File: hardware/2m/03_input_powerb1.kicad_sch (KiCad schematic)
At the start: 11 parts, among them Q303 MMBT3904,215

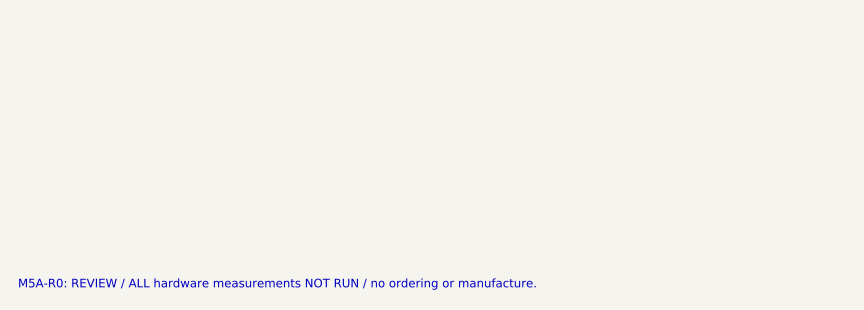
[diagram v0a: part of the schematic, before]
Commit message: Preserve M5A-R1 VHF electrical candidate and review evidence
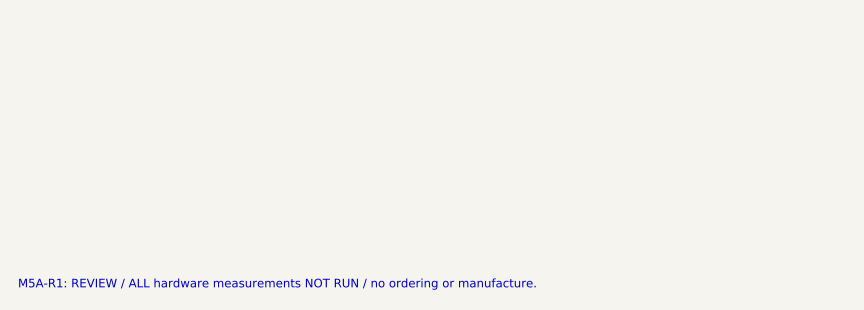
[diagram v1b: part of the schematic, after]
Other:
- note added: "M5A-R1: REVIEW / ALL hardware measurements NOT RUN / no ordering or manufacture."
- note removed: "M5A-R0: REVIEW / ALL hardware measurements NOT RUN / no ordering or manufacture."

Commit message: Preserve M5A-R3 historical transmitter schematic and review
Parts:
- C306: value 22u -> 1u; footprint Capacitor_SMD:C_1210_3225Metric -> Capacitor_SMD:C_0805_2012Metric; Engineering_Note (none) -> R3 switched-rail local1uF; original470uF bulk is upstream o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; MPN GRM32ER71E226KE15L -> CC0805KKX7R9BB105
- R309: Engineering_Note (none) -> 0.1ohm high-side normal-rail sense. Approx0.6A trip. Exact 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
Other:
- note added: "M5A-R3: REVIEW / ALL hardware measurements NOT RUN / no ordering or manufacture."
- note added: "R3: no RF/analog/thermal hardware validation. Original RF attribution and open procurement in M5A_R3 documents."
- note removed: "M5A-R1: REVIEW / ALL hardware measurements NOT RUN / no ordering or manufacture."

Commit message: Preserve M5A-R4 economical VHF electrical review baseline
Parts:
- C306: value 1u -> 100n; footprint Capacitor_SMD:C_0805_2012Metric -> Capacitor_SMD:C_0603_1608Metric; Engineering_Note R3 switched-rail local1uF; original470uF bulk is upstream o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 -> Protected9V local bypass; converter bulk upstream, driver r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; MPN CC0805KKX7R9BB105 -> CC0603KRX7R8BB104
- R309: Engineering_Note 0.1ohm high-side normal-rail sense. Approx0.6A trip. Exact 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 -> High-side0.1ohm sense; nominal1.80A analog trip retained. V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
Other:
- note added: "M5A-R4: REVIEW / ALL hardware measurements NOT RUN / no ordering or manufacture."
- note added: "M5A-R4: hardware measurements NOT_RUN; source/reference and simplification in R4 documents."
- note removed: "M5A-R3: REVIEW / ALL hardware measurements NOT RUN / no ordering or manufacture."
- note removed: "R3: no RF/analog/thermal hardware validation. Original RF attribution and open procurement in M5A_R3 documents."

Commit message: Preserve M5B-E1 integrated RF2M evaluation baseline
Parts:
- R309: value 0.1 -> 0.068; Engineering_Note High-side0.1ohm sense; nominal1.80A analog trip retained. V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 -> M5B confirmed current-protection correction:.068ohm1percent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; MPN OPEN 0.1ohm 1% 1W Kelvin layout -> WSL2512R0680FEA
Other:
- note added: "M5B-E1 / integrated evaluation PCB / NOT RELEASED / hardware tests NOT_RUN"
- note added: "M5B-E1: REVIEW / ALL hardware measurements NOT RUN / no ordering or manufacture."
- note removed: "M5A-R4: REVIEW / ALL hardware measurements NOT RUN / no ordering or manufacture."
- note removed: "M5A-R4: hardware measurements NOT_RUN; source/reference and simplification in R4 documents."

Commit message: Implement M5B-E3 standard JLCPCB RF2M evaluation board
Recalculate and implement 1.6 mm / 1 oz RF geometry, power copper, thermal vias, connector holes and manufacturing legend. Preserve electrical functions and population variants. Add native-geometry DFM, regression checks and fresh native/fabrication review archives. CAD milestone only; no manufacturing or operational release.
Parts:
- C306, C307: footprint Capacitor_SMD:C_0603_1608Metric -> ARDF_2M:C_0603_1608Metric_E3
- D304: footprint Diode_SMD:D_SOD-123F -> ARDF_2M:D_SOD-123F_E3
- Q303: footprint Package_TO_SOT_SMD:SOT-23 -> ARDF_2M:SOT-23_E3
- R306, R307, R308: footprint Resistor_SMD:R_0603_1608Metric -> ARDF_2M:R_0603_1608Metric_E3
- R309: footprint Resistor_SMD:R_2512_6332Metric -> ARDF_2M:R_2512_6332Metric_E3
- TP301, TP302, TP303: footprint TestPoint:TestPoint_Pad_D1.0mm -> ARDF_2M:TestPoint_Pad_D1.0mm_E3
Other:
- note added: "M5B-E3 / integrated evaluation PCB / NOT RELEASED / hardware tests NOT_RUN"
- note added: "M5B-E3: REVIEW / ALL hardware measurements NOT RUN / no ordering or manufacture."
- note removed: "M5B-E1 / integrated evaluation PCB / NOT RELEASED / hardware tests NOT_RUN"
- note removed: "M5B-E1: REVIEW / ALL hardware measurements NOT RUN / no ordering or manufacture."

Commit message: Implement M5B-E4 thermal candidate with source-joint assembly hold
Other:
- note added: "M5B-E4 / integrated evaluation PCB / NOT RELEASED / hardware tests NOT_RUN"
- note added: "M5B-E4: REVIEW / ALL hardware measurements NOT RUN / no ordering or manufacture."
- note removed: "M5B-E3 / integrated evaluation PCB / NOT RELEASED / hardware tests NOT_RUN"
- note removed: "M5B-E3: REVIEW / ALL hardware measurements NOT RUN / no ordering or manufacture."

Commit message: Implement M5B-E4R1 source-joint prototype candidate
Replace source mask islands with a controlled open-via hybrid and native-derived local stencil. Preserve standard JLCPCB and RF circuitry. Add assembly qualification, thermal convergence and adverse sensitivities, native DFM/mutation checks and fresh review exports. Conservative 110 C target is missed; 125 C physical gate stays open. No acceptance tag or manufacturing authorization.
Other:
- note added: "M5B-E4R1R1R1 / integrated evaluation PCB / NOT RELEASED / hardware tests NOT_RUN"
- note added: "M5B-E4R1R1R1: REVIEW / ALL hardware measurements NOT RUN / no ordering or manufacture."
- note removed: "M5B-E4 / integrated evaluation PCB / NOT RELEASED / hardware tests NOT_RUN"
- note removed: "M5B-E4: REVIEW / ALL hardware measurements NOT RUN / no ordering or manufacture."

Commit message: M5B-E5: compact RF2M to the shared 150x110 mm platform
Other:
- note added: "M5B-E5R1R1 / integrated evaluation PCB / NOT RELEASED / hardware tests NOT_RUN"
- note added: "M5B-E5R1R1: REVIEW / ALL hardware measurements NOT RUN / no ordering or manufacture."
- note removed: "M5B-E4R1R1R1 / integrated evaluation PCB / NOT RELEASED / hardware tests NOT_RUN"
- note removed: "M5B-E4R1R1R1: REVIEW / ALL hardware measurements NOT RUN / no ordering or manufacture."
